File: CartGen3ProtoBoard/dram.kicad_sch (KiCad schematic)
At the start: 1 part, among them U4 AS4C32M8SA

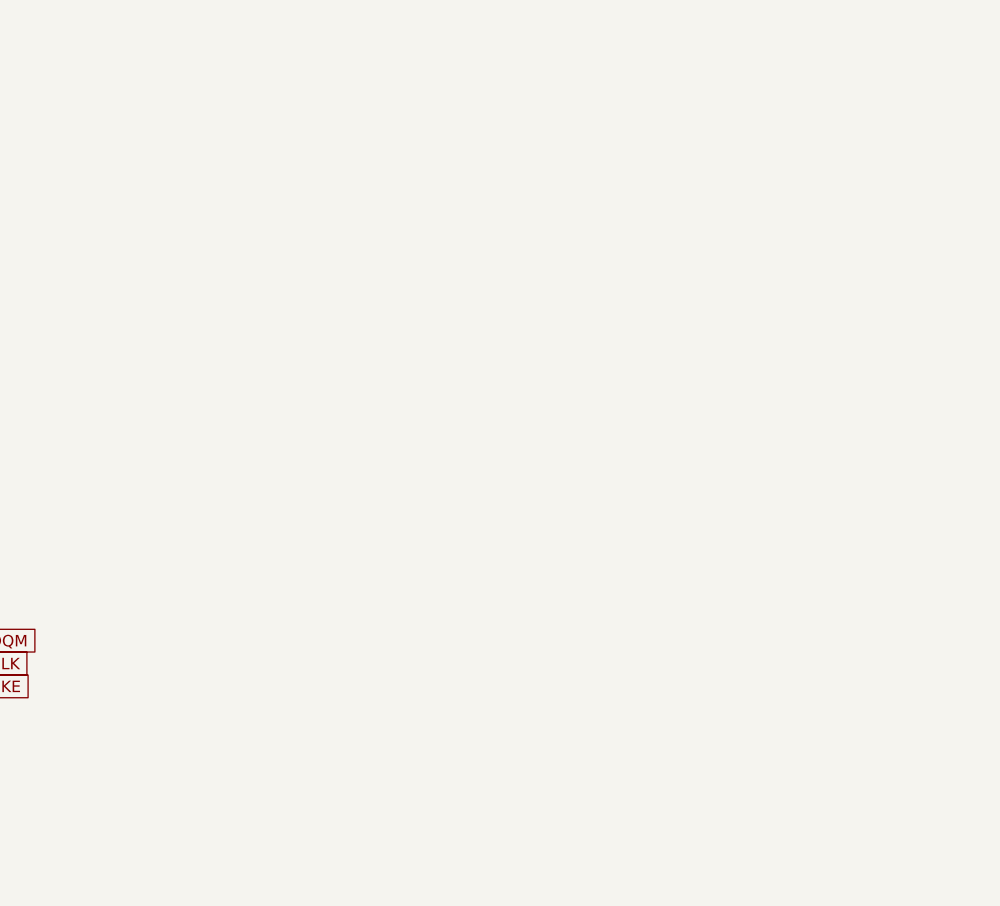
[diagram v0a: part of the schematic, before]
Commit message: Added bypass capacitors to prototype
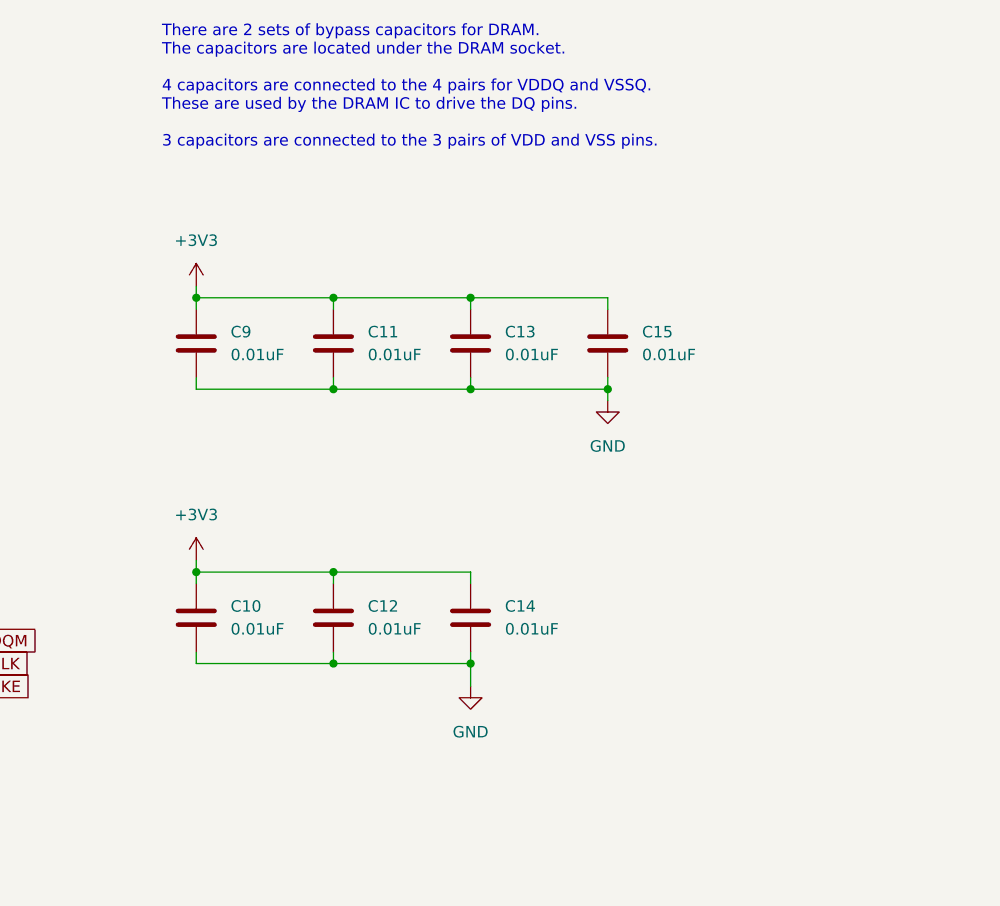
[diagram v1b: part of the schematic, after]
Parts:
- added C10, C11, C12, C13, C14, C15, C9: 0.01uF, symbol Device:C
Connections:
- net +3V3: now also C10.1, C11.1, C12.1, C13.1, C14.1, C15.1, C9.1
- net GND: now also C10.2, C11.2, C12.2, C13.2, C14.2, C15.2, C9.2
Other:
- note added: "There are 2 sets of bypass capacitors for DRAM. The capacitors are located under the DRAM socket. 4 capacitors are connected to the 4 pairs for VDDQ and VSSQ. These are used by the DRAM IC to drive the DQ pins. 3 capacitors are connected to the 3 pairs of VDD and VSS pins."
